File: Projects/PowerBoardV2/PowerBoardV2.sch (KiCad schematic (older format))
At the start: 18 parts, among them P1 ATX-20, P10 CONN_2, P11 CONN_2, P12 CONN_2, P13 CONN_2, P14 CONN_2, P15 CONN_2, P16 CONN_2, P17 CONN_2, P18 CONN_2, P2 CONN_2, P3 CONN_2, P4 CONN_2, P5 CONN_2, P6 CONN_2, P7 CONN_2, P8 CONN_2, P9 CONN_2

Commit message: Updated Power Distribution Board and refs
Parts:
- P1: footprint USSTPARTS:ATX20 -> USST-footprints:ATX20
- P10, P11, P12, P14, P15, P16, P2, P3, P4, P5, P7, P8: footprint Connect:bornier2 -> USST-footprints:Molex_39531_1002
- P13, P17, P18, P6, P9: footprint USSTPARTS:PhoenixContact1770539 -> USST-footprints:Phoenix_Contact_1770539
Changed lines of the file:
@@
 LIBS:contrib
 LIBS:valves
+LIBS:USST-parts
 LIBS:PowerBoardV2-cache
 EELAYER 25 0
@@
 F 0 "P1" H 2500 3200 60  0000 C CNN
 F 1 "ATX-20" H 2500 1900 60  0000 C CNN
-F 2 "USSTPARTS:ATX20" V 2400 2600 60  0001 C CNN
+F 2 "USST-footprints:ATX20" V 2400 2600 60  0001 C CNN
 F 3 "" V 2400 2600 60  0000 C CNN
 	1    2500 2500
@@
 F 0 "P2" V 2350 1400 40  0000 C CNN
 F 1 "CONN_2" V 2450 1400 40  0000 C CNN
-F 2 "Connect:bornier2" H 2400 1400 60  0001 C CNN
+F 2 "USST-footprints:Molex_39531_1002" H 2400 1400 60  0001 C CNN
 F 3 "" H 2400 1400 60  0000 C CNN
 	1    2400 1400
@@
 F 0 "P3" V 5200 1950 40  0000 C CNN
 F 1 "CONN_2" V 5300 1950 40  0000 C CNN
-F 2 "Connect:bornier2" H 5250 1950 60  0001 C CNN
+F 2 "USST-footprints:Molex_39531_1002" H 5250 1950 60  0001 C CNN
 F 3 "" H 5250 1950 60  0000 C CNN
 	1    5250 1950
@@
 F 0 "P7" V 5650 1950 40  0000 C CNN
 F 1 "CONN_2" V 5750 1950 40  0000 C CNN
-F 2 "Connect:bornier2" H 5700 1950 60  0001 C CNN
+F 2 "USST-footprints:Molex_39531_1002" H 5700 1950 60  0001 C CNN
 F 3 "" H 5700 1950 60  0000 C CNN
 	1    5700 1950
@@
 F 0 "P10" V 6100 1950 40  0000 C CNN
 F 1 "CONN_2" V 6200 1950 40  0000 C CNN
-F 2 "Connect:bornier2" H 6150 1950 60  0001 C CNN
+F 2 "USST-footprints:Molex_39531_1002" H 6150 1950 60  0001 C CNN
 F 3 "" H 6150 1950 60  0000 C CNN
 	1    6150 1950
@@
 F 0 "P14" V 6550 1950 40  0000 C CNN
 F 1 "CONN_2" V 6650 1950 40  0000 C CNN
-F 2 "Connect:bornier2" H 6600 1950 60  0001 C CNN
+F 2 "USST-footprints:Molex_39531_1002" H 6600 1950 60  0001 C CNN
 F 3 "" H 6600 1950 60  0000 C CNN
 	1    6600 1950
@@
 F 0 "P4" V 5200 2900 40  0000 C CNN
 F 1 "CONN_2" V 5300 2900 40  0000 C CNN
-F 2 "Connect:bornier2" H 5250 2900 60  0001 C CNN
+F 2 "USST-footprints:Molex_39531_1002" H 5250 2900 60  0001 C CNN
 F 3 "" H 5250 2900 60  0000 C CNN
 	1    5250 2900
@@
 F 0 "P8" V 5650 2900 40  0000 C CNN
 F 1 "CONN_2" V 5750 2900 40  0000 C CNN
-F 2 "Connect:bornier2" H 5700 2900 60  0001 C CNN
+F 2 "USST-footprints:Molex_39531_1002" H 5700 2900 60  0001 C CNN
 F 3 "" H 5700 2900 60  0000 C CNN
 	1    5700 2900
@@
 F 0 "P11" V 6100 2900 40  0000 C CNN
 F 1 "CONN_2" V 6200 2900 40  0000 C CNN
-F 2 "Connect:bornier2" H 6150 2900 60  0001 C CNN
+F 2 "USST-footprints:Molex_39531_1002" H 6150 2900 60  0001 C CNN
 F 3 "" H 6150 2900 60  0000 C CNN
 	1    6150 2900
@@
 F 0 "P15" V 6550 2900 40  0000 C CNN
 F 1 "CONN_2" V 6650 2900 40  0000 C CNN
-F 2 "Connect:bornier2" H 6600 2900 60  0001 C CNN
+F 2 "USST-footprints:Molex_39531_1002" H 6600 2900 60  0001 C CNN
 F 3 "" H 6600 2900 60  0000 C CNN
 	1    6600 2900
@@
 F 0 "P5" V 5200 3850 40  0000 C CNN
 F 1 "CONN_2" V 5300 3850 40  0000 C CNN
-F 2 "Connect:bornier2" H 5250 3850 60  0001 C CNN
+F 2 "USST-footprints:Molex_39531_1002" H 5250 3850 60  0001 C CNN
 F 3 "" H 5250 3850 60  0000 C CNN
 	1    5250 3850
@@
 F 0 "P12" V 6100 3850 40  0000 C CNN
 F 1 "CONN_2" V 6200 3850 40  0000 C CNN
-F 2 "Connect:bornier2" H 6150 3850 60  0001 C CNN
+F 2 "USST-footprints:Molex_39531_1002" H 6150 3850 60  0001 C CNN
 F 3 "" H 6150 3850 60  0000 C CNN
 	1    6150 3850
@@
 F 0 "P16" V 6550 3850 40  0000 C CNN
 F 1 "CONN_2" V 6650 3850 40  0000 C CNN
-F 2 "Connect:bornier2" H 6600 3850 60  0001 C CNN
+F 2 "USST-footprints:Molex_39531_1002" H 6600 3850 60  0001 C CNN
 F 3 "" H 6600 3850 60  0000 C CNN
 	1    6600 3850
@@
 F 0 "P6" V 5250 5000 40  0000 C CNN
 F 1 "CONN_2" V 5350 5000 40  0000 C CNN
-F 2 "USSTPARTS:PhoenixContact1770539" H 5300 5000 60  0001 C CNN
+F 2 "USST-footprints:Phoenix_Contact_1770539" H 5300 5000 60  0001 C CNN
 F 3 "" H 5300 5000 60  0000 C CNN
 	1    5300 5000
@@
 F 0 "P9" V 5700 5000 40  0000 C CNN
 F 1 "CONN_2" V 5800 5000 40  0000 C CNN
-F 2 "USSTPARTS:PhoenixContact1770539" H 5750 5000 60  0001 C CNN
+F 2 "USST-footprints:Phoenix_Contact_1770539" H 5750 5000 60  0001 C CNN
 F 3 "" H 5750 5000 60  0000 C CNN
 	1    5750 5000
@@
 F 0 "P13" V 6150 5000 40  0000 C CNN
 F 1 "CONN_2" V 6250 5000 40  0000 C CNN
-F 2 "USSTPARTS:PhoenixContact1770539" H 6200 5000 60  0001 C CNN
+F 2 "USST-footprints:Phoenix_Contact_1770539" H 6200 5000 60  0001 C CNN
 F 3 "" H 6200 5000 60  0000 C CNN
 	1    6200 5000
@@
 F 0 "P17" V 6600 5000 40  0000 C CNN
 F 1 "CONN_2" V 6700 5000 40  0000 C CNN
-F 2 "USSTPARTS:PhoenixContact1770539" H 6650 5000 60  0001 C CNN
+F 2 "USST-footprints:Phoenix_Contact_1770539" H 6650 5000 60  0001 C CNN
 F 3 "" H 6650 5000 60  0000 C CNN
 	1    6650 5000
@@
 F 0 "P18" V 7800 5000 40  0000 C CNN
 F 1 "CONN_2" V 7900 5000 40  0000 C CNN
-F 2 "USSTPARTS:PhoenixContact1770539" H 7850 5000 60  0001 C CNN
+F 2 "USST-footprints:Phoenix_Contact_1770539" H 7850 5000 60  0001 C CNN
 F 3 "" H 7850 5000 60  0000 C CNN
 	1    7850 5000

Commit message: Almost done just need to add silk screen stuff
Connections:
- net VBAT_IN is gone; now on net VBAT: P18.2 (PM)
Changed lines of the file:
@@
 	8100 5650 8200 5650
 Text GLabel 8200 5450 2    60   Input ~ 0
-VBAT_IN
+VBAT
 Text GLabel 8200 5650 2    60   Input ~ 0
 GND
@@
 	9000 2700 8850 2700
 Text GLabel 8850 2700 0    60   Input ~ 0
-VBAT_IN
+VBAT
 Wire Wire Line
 	9000 2850 8850 2850

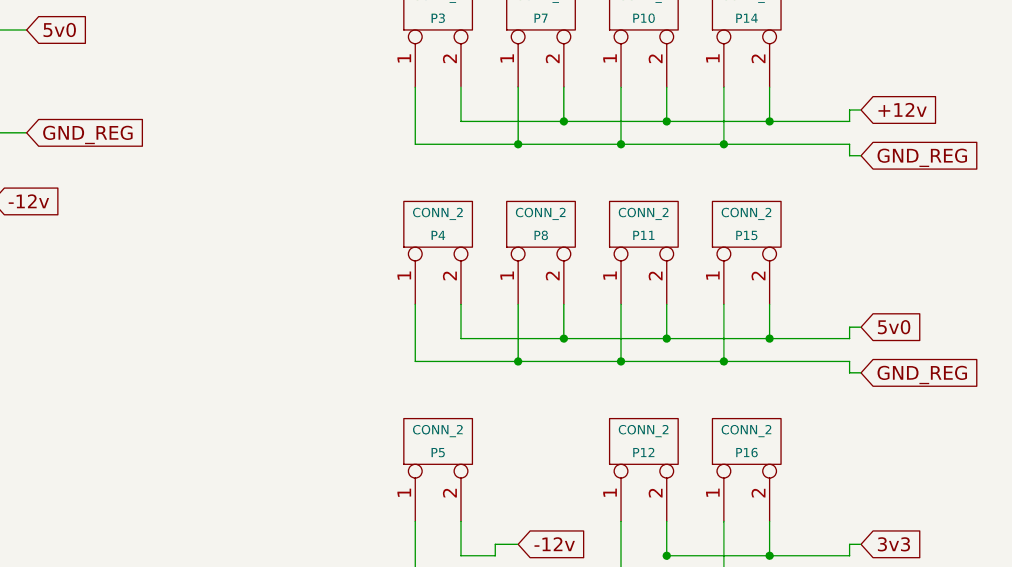
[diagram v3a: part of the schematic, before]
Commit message: added BOM for backplane
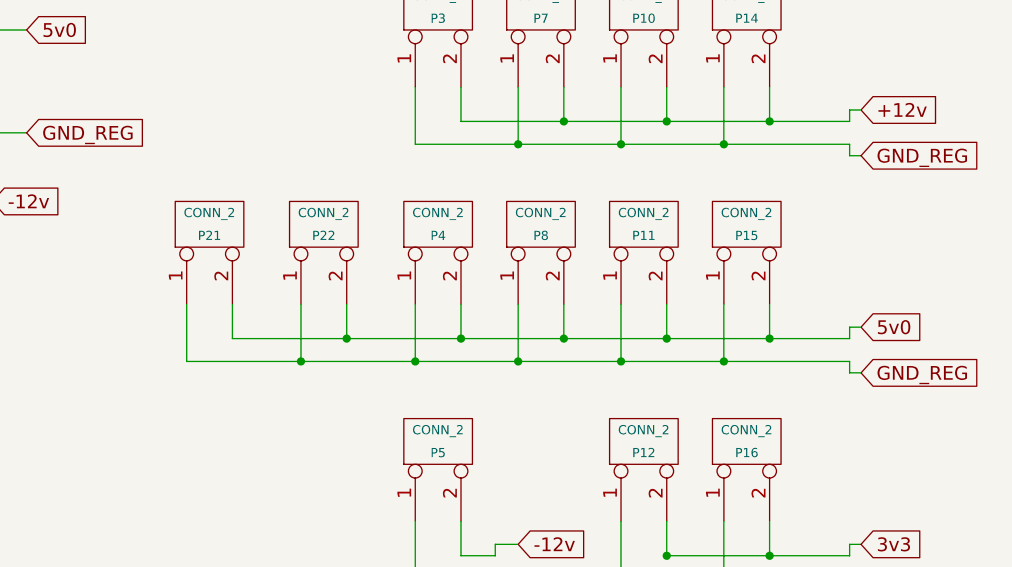
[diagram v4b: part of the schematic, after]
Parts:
- added P21, P22: CONN_2, USST-footprints:Molex_39531_1002, symbol CONN_2
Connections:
- net 5v0: now also P21.2 (PM), P22.2 (PM)
- net GND_REG: now also P21.1 (P1), P22.1 (P1)
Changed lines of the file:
@@
 EESchema Schematic File Version 2
+LIBS:PowerBoardV2-rescue
 LIBS:power
 LIBS:device
@@
 	5150 3250 5150 3500
 Wire Wire Line
-	5150 3500 7050 3500
+	4150 3500 7050 3500
 Wire Wire Line
 	6500 3500 6500 3250
@@
 	5350 3250 5350 3400
 Wire Wire Line
-	5350 3400 7050 3400
+	4350 3400 7050 3400
 Wire Wire Line
 	5800 3400 5800 3250
@@
 Text GLabel 8850 3450 0    60   Input ~ 0
 VLOG
+$Comp
+L CONN_2 P22
+U 1 1 58AE4A1E
+P 4750 2900
+F 0 "P22" V 4700 2900 40  0000 C CNN
+F 1 "CONN_2" V 4800 2900 40  0000 C CNN
+F 2 "USST-footprints:Molex_39531_1002" H 4750 2900 60  0001 C CNN
+F 3 "" H 4750 2900 60  0000 C CNN
+	1    4750 2900
+	0    -1   -1   0
+$EndComp
+$Comp
+L CONN_2 P21
+U 1 1 58AE4AF3
+P 4250 2900
+F 0 "P21" V 4200 2900 40  0000 C CNN
+F 1 "CONN_2" V 4300 2900 40  0000 C CNN
+F 2 "USST-footprints:Molex_39531_1002" H 4250 2900 60  0001 C CNN
+F 3 "" H 4250 2900 60  0000 C CNN
+	1    4250 2900
+	0    -1   -1   0
+$EndComp
+Wire Wire Line
+	4850 3250 4850 3400
+Connection ~ 5350 3400
+Wire Wire Line
+	4350 3250 4350 3400
+Connection ~ 4850 3400
+Wire Wire Line
+	4150 3500 4150 3250
+Connection ~ 5150 3500
+Wire Wire Line
+	4650 3250 4650 3500
+Connection ~ 4650 3500
 $EndSCHEMATC
